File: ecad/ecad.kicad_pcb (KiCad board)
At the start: 4 copper layers, 130.5 x 110.5 mm, 122 parts, among them J1 JTAG, J2 USB_C, J3 Display, Q2 SS8050, SW1 Kailh choc v2, SW10 RotaryEncoder_Switch, SW11 RotaryEncoder_Switch, SW12 Kailh choc v2, SW13 Kailh choc v2, SW14 Kailh choc v2, SW15 RESET, SW16 Kailh choc v2, SW17 Kailh choc v2, SW18 Kailh choc v2, SW19 Kailh choc v2, SW2 Kailh choc v2, SW20 Kailh choc v2, SW21 Kailh choc v2, SW22 Kailh choc v2, SW23 Kailh choc v2, SW24 Kailh choc v2, SW25 Kailh choc v2, SW3 Kailh choc v2, SW4 Kailh choc v2, SW5 Kailh choc v2, SW6 Kailh choc v2, SW7 Kailh choc v2, SW8 Kailh choc v2, SW9 Kailh choc v2, U1 AP2112K-3.3, U2 RP2040, U4 SN74LV1T34DBV, U5 W25Q128JVP, Y1 12MHz

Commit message: fix(ecad): change screw placement and rounded corners
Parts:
- moved D29 104.7 mm to (190.7, 75.4)
- moved H1 70.0 mm to (125.7, 96.4)
- moved H3 68.5 mm to (125.7, 153.4)
- moved D46 34.0 mm to (205.8, 75.2), turned to 90 degrees
- moved H2 33.7 mm to (87.7, 96.4)
- moved H4 30.4 mm to (87.7, 153.4)
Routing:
- net GND: track 64.2 -> 64.9 mm, vias 43 -> 44
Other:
- outline, holes or cut-outs redrawn

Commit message: feat(ecad): ws2812b placement and routing
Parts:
- removed D15, D16, D20, D24, D28, D44: WS2812B-2020, LED_SMD:LED_WS2812B-2020_PLCC4_2.0x2.0mm
- added H10: MountingHole, MountingHole:MountingHole_2.2mm_M2_DIN965, F.Cu at (148.9, 169.8)
- added H11: MountingHole, MountingHole:MountingHole_2.2mm_M2_DIN965, F.Cu at (71.3, 73.4)
- added H12: MountingHole, MountingHole:MountingHole_2.2mm_M2_DIN965, F.Cu at (148.9, 73.4)
- added H9: MountingHole, MountingHole:MountingHole_2.2mm_M2_DIN965, F.Cu at (186.6, 100.2)
- moved D27 313.1 mm to (66.2, 78.8)
- moved D19 312.2 mm to (66.2, 121.6)
- moved D23 310.1 mm to (66.2, 99.8)
- moved D31 301.8 mm to (76.7, 174.9), turned to 0 degrees
- moved D30 274.3 mm to (97.7, 174.9), turned to 0 degrees
- moved D26 236.3 mm to (118.7, 174.9), turned to 0 degrees
- moved D22 199.9 mm to (138.2, 174.9), turned to 0 degrees
- moved D18 162.2 mm to (159.2, 174.9), turned to 0 degrees
- moved D47 154.4 mm to (66.2, 164.4), turned to -90 degrees
- moved D43 152.2 mm to (66.2, 143.4), turned to -90 degrees
- moved D42 146.0 mm to (76.7, 68.2)
- moved D14 124.9 mm to (180.2, 174.9), turned to 0 degrees
- moved D48 123.4 mm to (97.7, 68.2)
- moved D13 107.8 mm to (190.7, 164.4)
- moved D41 106.7 mm to (117.2, 68.2)
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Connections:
- D17 pad 1: Net-(D17-DOUT) -> Net-(D13-DIN)
- D23 pad 1: Net-(D19-DIN) -> Net-(D23-DOUT)
- D23 pad 3: Net-(D23-DIN) -> Net-(D19-DOUT)
- D27 pad 1: Net-(D23-DIN) -> Net-(D27-DOUT)
- D27 pad 3: Net-(D27-DIN) -> Net-(D23-DOUT)
- D31 pad 1: Net-(D27-DIN) -> Net-(D31-DOUT)
- D41 pad 3: Net-(D17-DOUT) -> Net-(D41-DIN)
- D42 pad 1: Net-(D13-DIN) -> Net-(D42-DOUT)
- D42 pad 2: unconnected-(D42-VSS-Pad2) -> GND
- D42 pad 3: Net-(D42-DIN) -> Net-(D27-DOUT)
- D43 pad 1: Net-(D43-DOUT) -> Net-(D19-DIN)
- D43 pad 3: Net-(D19-DOUT) -> Net-(D43-DIN)
- D46 pad 1: Net-(D42-DIN) -> unconnected-(D46-DOUT-Pad1)
- D46 pad 2: unconnected-(D46-VSS-Pad2) -> GND
- D47 pad 1: Net-(D47-DOUT) -> Net-(D43-DIN)
- D47 pad 3: Net-(D43-DOUT) -> Net-(D31-DOUT)
- D48 pad 1: Net-(D44-DIN) -> Net-(D41-DIN)
- D48 pad 3: Net-(D47-DOUT) -> Net-(D42-DOUT)
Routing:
- net +5V: track 8.41 -> 479.1 mm
- net Net-(D17-DIN): track 0.00 -> 20.5 mm
- net Net-(D19-DIN): track 0.00 -> 20.5 mm
- net Net-(D21-DIN): track 0.00 -> 20.5 mm
- net Net-(D19-DOUT): track 0.00 -> 20.5 mm
- net Net-(D43-DIN): track 0.00 -> 19.6 mm
- net Net-(D13-DIN): track 0.00 -> 19.6 mm
- net Net-(D42-DOUT): track 0.00 -> 19.6 mm
- net Net-(D41-DOUT): track 0.00 -> 19.6 mm
- net Net-(D30-DOUT): track 0.00 -> 19.6 mm
- net Net-(D26-DOUT): track 0.00 -> 19.6 mm
- net Net-(D45-DOUT): track 0.00 -> 19.6 mm
- net Net-(D25-DIN): track 0.00 -> 19.6 mm
- net Net-(D23-DOUT): track 0.00 -> 19.6 mm
- net Net-(D18-DOUT): track 0.00 -> 19.6 mm
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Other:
- board size 130.5 x 110.5 mm -> 130.5 x 112.7 mm

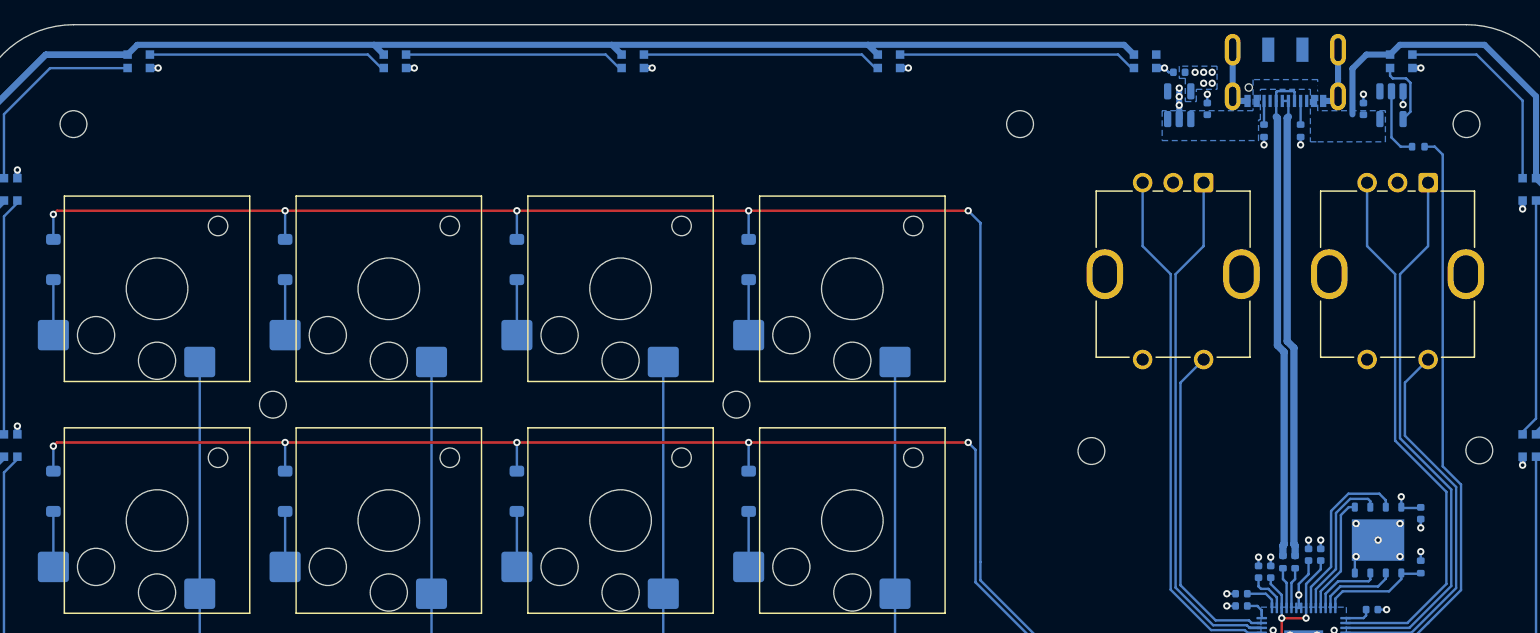
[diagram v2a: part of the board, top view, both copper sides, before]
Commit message: fix(ecad): change usb connector
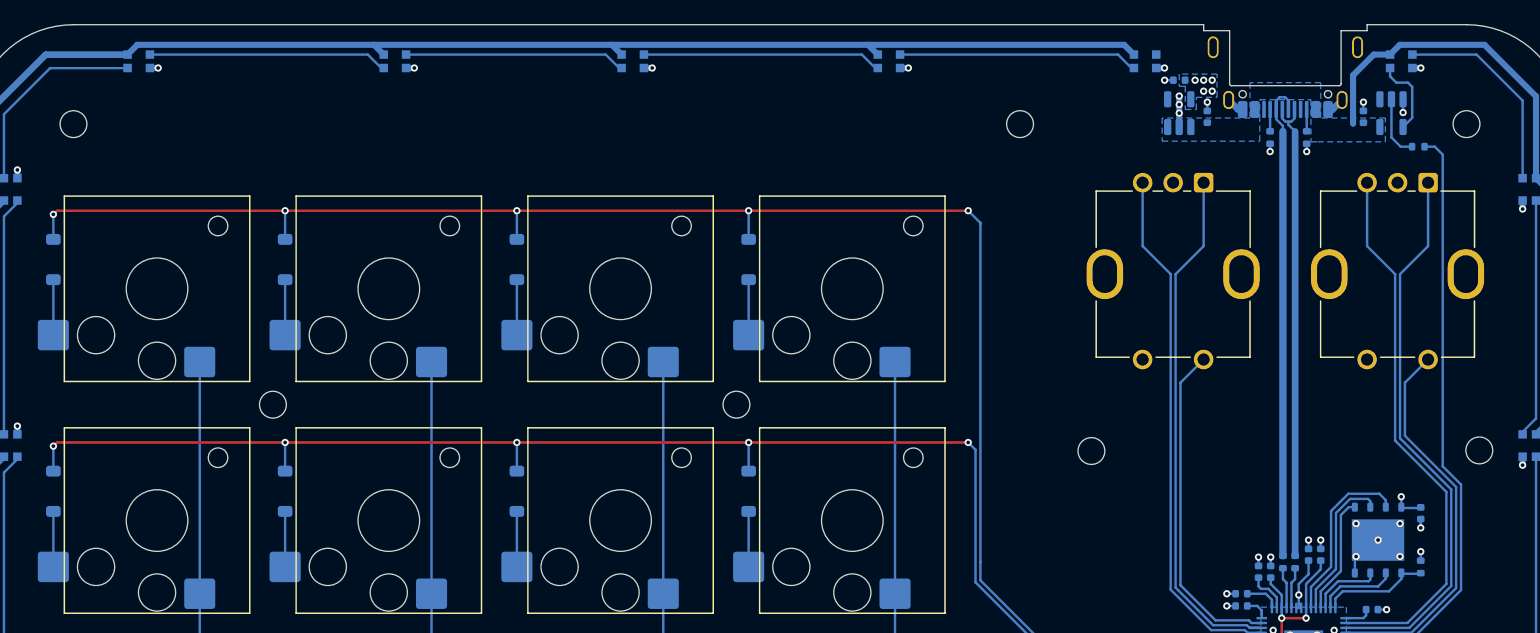
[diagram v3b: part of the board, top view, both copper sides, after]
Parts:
- J2: footprint Connector_USB:USB_C_Receptacle_JAE_DX07S016JA1R1500 -> Connector_USB:USB_C_Receptacle_Amphenol_12401948E412A
- moved J2 1.35 mm to (170.7, 67.1)
- moved R5 0.74 mm to (169.4, 74.5)
- moved R6 0.74 mm to (172.4, 74.5)
- moved U1 0.65 mm to (162.0, 72.5)
- moved U4 0.65 mm to (179.4, 72.5)
- moved C1 0.65 mm to (164.3, 72.8)
- moved C18 0.65 mm to (177.1, 72.8)
- moved C2 0.65 mm to (162.0, 69.8)
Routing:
- net GND: track 79.4 -> 71.8 mm, vias 64 -> 65
- net Net-(J2-D--PadA7): track 40.6 -> 39.5 mm
- net Net-(D32-DIN): track 5.77 -> 6.46 mm
- net Net-(U4-A): track 5.80 -> 5.15 mm
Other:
- outline, holes or cut-outs redrawn

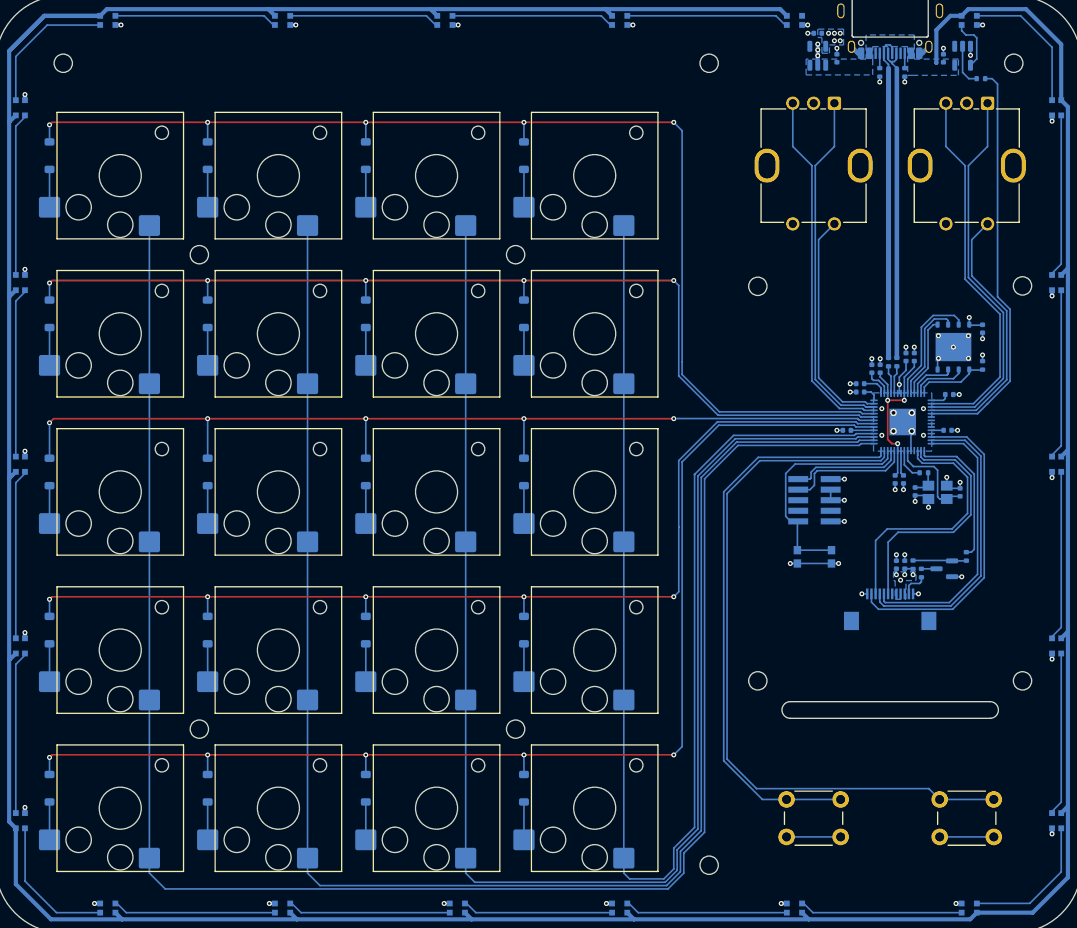
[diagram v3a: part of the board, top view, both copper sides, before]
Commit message: fix(ecad): change screw holes size
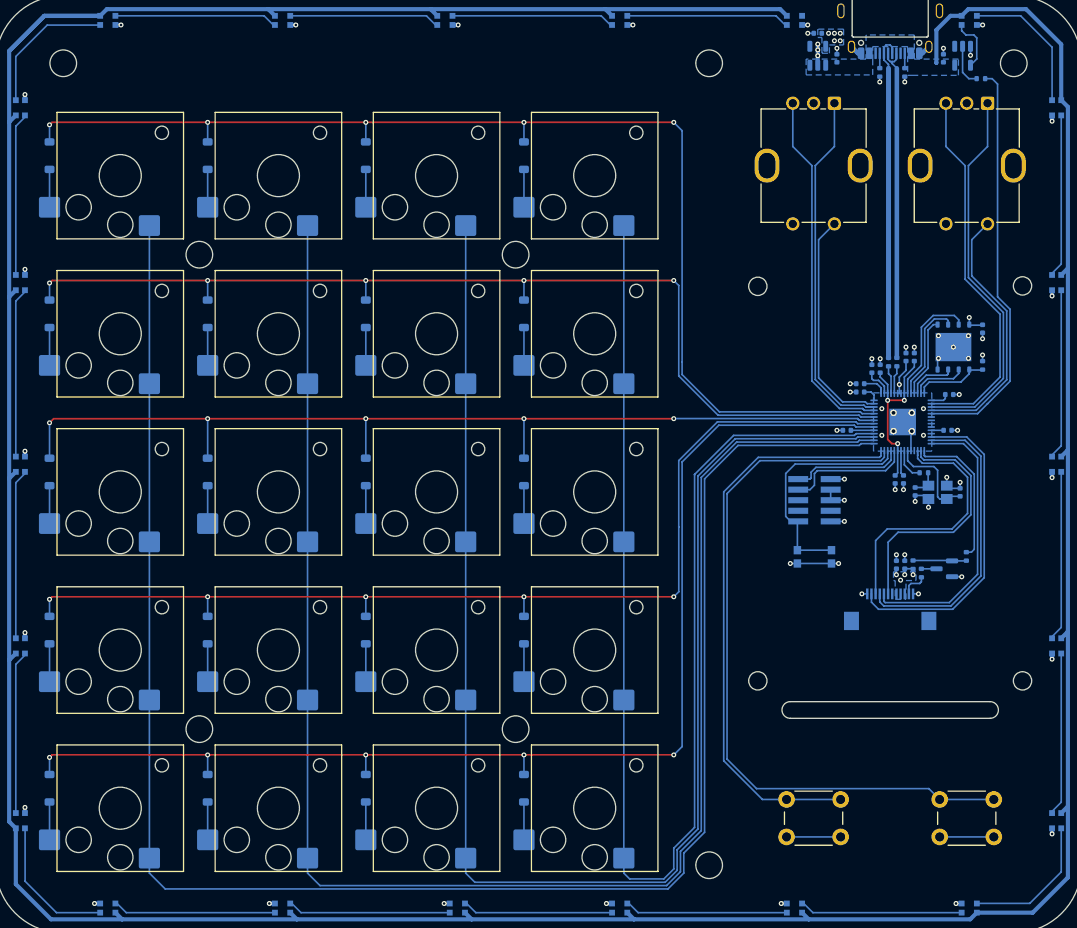
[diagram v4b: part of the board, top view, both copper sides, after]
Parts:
- H1, H10, H11, H12, H2, H3, H4, H5: footprint MountingHole:MountingHole_2.2mm_M2_DIN965 -> MountingHole:MountingHole_3.2mm_M3_DIN965
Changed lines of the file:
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@@
 	(net 104 "Net-(D43-DIN)")
 	(net 105 "Net-(D45-DOUT)")
-	(footprint "MountingHole:MountingHole_2.2mm_M2_DIN965"
+	(footprint "MountingHole:MountingHole_3.2mm_M3_DIN965"
 		(locked yes)
 		(layer "F.Cu")
 		(at 185.55 73.4)
-		(descr "Mounting Hole 2.2mm, M2, no annular, generated by kicad-footprint-generator mountinghole.py")
-		(tags "mountinghole M2 DIN965")
+		(descr "Mounting Hole 3.2mm, M3, no annular, generated by kicad-footprint-generator mountinghole.py")
+		(tags "mountinghole M3 DIN965")
 		(property "Reference" "H5"
-			(at 0 -2.85 0)
+			(at 0 -3.75 0)
 			(layer "F.SilkS")
 			(hide yes)
@@
 		)
 		(property "Value" "MountingHole"
-			(at 0 2.85 0)
+			(at 0 3.75 0)
 			(layer "F.Fab")
 			(effects
@@
 		(fp_circle
 			(center 0 0)
-			(end 1.9 0)
+			(end 2.8 0)
 			(stroke
 				(width 0.15)
@@
 		(fp_circle
 			(center 0 0)
-			(end 2.15 0)
+			(end 3.05 0)
 			(stroke
 				(width 0.05)
@@
 			(effects
 				(font
-					(size 0.95 0.95)
-					(thickness 0.14)
+					(size 1 1)
+					(thickness 0.15)
 				)
 			)
@@
 		(pad "" np_thru_hole circle
 			(at 0 0)
-			(size 2.2 2.2)
-			(drill 2.2)
+			(size 3.2 3.2)
+			(drill 3.2)
 			(layers "*.Cu" "*.Mask")
 		)
@@
 		)
 	)
-	(footprint "MountingHole:MountingHole_2.2mm_M2_DIN965"
+	(footprint "MountingHole:MountingHole_3.2mm_M3_DIN965"
 		(locked yes)
 		(layer "F.Cu")
 		(at 148.95 169.75)
-		(descr "Mounting Hole 2.2mm, M2, no annular, generated by kicad-footprint-generator mountinghole.py")
-		(tags "mountinghole M2 DIN965")
+		(descr "Mounting Hole 3.2mm, M3, no annular, generated by kicad-footprint-generator mountinghole.py")
+		(tags "mountinghole M3 DIN965")
 		(property "Reference" "H10"
-			(at 0 -2.85 0)
+			(at 0 -3.75 0)
 			(layer "F.SilkS")
 			(hide yes)
@@
 		)
 		(property "Value" "MountingHole"
-			(at 0 2.85 0)
+			(at 0 3.75 0)
 			(layer "F.Fab")
 			(effects
@@
 		(fp_circle
 			(center 0 0)
-			(end 1.9 0)
+			(end 2.8 0)
 			(stroke
 				(width 0.15)
@@
 		(fp_circle
 			(center 0 0)
-			(end 2.15 0)
+			(end 3.05 0)
 			(stroke
 				(width 0.05)
@@
 			(layer "F.CrtYd")
 		)
+		(fp_text user "${REFERENCE}"
+			(at 0 0 0)
+			(layer "F.Fab")
+			(effects
+				(font
+					(size 1 1)
+					(thickness 0.15)
+				)
+			)
+		)
 		(pad "" np_thru_hole circle
 			(at 0 0)
-			(size 2.2 2.2)
-			(drill 2.2)
+			(size 3.2 3.2)
+			(drill 3.2)
 			(layers "*.Cu" "*.Mask")
 		)
@@
 		)
 	)
-	(footprint "MountingHole:MountingHole_2.2mm_M2_DIN965"
+	(footprint "MountingHole:MountingHole_3.2mm_M3_DIN965"
 		(locked yes)
 		(layer "F.Cu")
 		(at 71.35 73.4)
-		(descr "Mounting Hole 2.2mm, M2, no annular, generated by kicad-footprint-generator mountinghole.py")
-		(tags "mountinghole M2 DIN965")
+		(descr "Mounting Hole 3.2mm, M3, no annular, generated by kicad-footprint-generator mountinghole.py")
+		(tags "mountinghole M3 DIN965")
 		(property "Reference" "H11"
-			(at 0 -2.85 0)
+			(at 0 -3.75 0)
 			(layer "F.SilkS")
 			(hide yes)
@@
 		)
 		(property "Value" "MountingHole"
-			(at 0 2.85 0)
+			(at 0 3.75 0)
 			(layer "F.Fab")
 			(effects
@@
 		(fp_circle
 			(center 0 0)
-			(end 1.9 0)
+			(end 2.8 0)
 			(stroke
 				(width 0.15)
@@
 		(fp_circle
 			(center 0 0)
-			(end 2.15 0)
+			(end 3.05 0)
 			(stroke
 				(width 0.05)
@@
 			(layer "F.CrtYd")
 		)
+		(fp_text user "${REFERENCE}"
+			(at 0 0 0)
+			(layer "F.Fab")
+			(effects
+				(font
+					(size 1 1)
+					(thickness 0.15)
+				)
+			)
+		)
 		(pad "" np_thru_hole circle
 			(at 0 0)
-			(size 2.2 2.2)
-			(drill 2.2)
+			(size 3.2 3.2)
+			(drill 3.2)
 			(layers "*.Cu" "*.Mask")
 		)
 		(embedded_fonts no)
 	)
-	(footprint "MountingHole:MountingHole_2.2mm_M2_DIN965"
+	(footprint "MountingHole:MountingHole_3.2mm_M3_DIN965"
 		(locked yes)
 		(layer "F.Cu")
 		(at 148.95 73.4)
-		(descr "Mounting Hole 2.2mm, M2, no annular, generated by kicad-footprint-generator mountinghole.py")
-		(tags "mountinghole M2 DIN965")
+		(descr "Mounting Hole 3.2mm, M3, no annular, generated by kicad-footprint-generator mountinghole.py")
+		(tags "mountinghole M3 DIN965")
 		(property "Reference" "H12"
-			(at 0 -2.85 0)
+			(at 0 -3.75 0)
 			(layer "F.SilkS")
 			(hide yes)
@@
 		)
 		(property "Value" "MountingHole"
-			(at 0 2.85 0)
+			(at 0 3.75 0)
 			(layer "F.Fab")
 			(effects
@@
 		(fp_circle
 			(center 0 0)
-			(end 1.9 0)
+			(end 2.8 0)
 			(stroke
 				(width 0.15)
@@
 		(fp_circle
 			(center 0 0)
-			(end 2.15 0)
+			(end 3.05 0)
 			(stroke
 				(width 0.05)
@@
 			(layer "F.CrtYd")
 		)
+		(fp_text user "${REFERENCE}"
+			(at 0 0 0)
+			(layer "F.Fab")
+			(effects
+				(font
+					(size 1 1)
+					(thickness 0.15)
+				)
+			)
+		)
 		(pad "" np_thru_hole circle
 			(at 0 0)
-			(size 2.2 2.2)
-			(drill 2.2)
+			(size 3.2 3.2)
+			(drill 3.2)
 			(layers "*.Cu" "*.Mask")
 		)
@@
 		)
 	)
-	(footprint "MountingHole:MountingHole_2.2mm_M2_DIN965"
+	(footprint "MountingHole:MountingHole_3.2mm_M3_DIN965"
 		(locked yes)
 		(layer "B.Cu")
 		(at 87.7 96.4 180)
-		(descr "Mounting Hole 2.2mm, M2, no annular, generated by kicad-footprint-generator mountinghole.py")
-		(tags "mountinghole M2 DIN965")
+		(descr "Mounting Hole 3.2mm, M3, no annular, generated by kicad-footprint-generator mountinghole.py")
+		(tags "mountinghole M3 DIN965")
 		(property "Reference" "H2"
-			(at 0 2.85 0)
+			(at 0 3.75 0)
 			(layer "B.SilkS")
 			(hide yes)
@@
 		)
 		(property "Value" "MountingHole"
-			(at 0 -2.85 0)
+			(at 0 -3.75 0)
 			(layer "B.Fab")
 			(effects
@@
 		(fp_circle
 			(center 0 0)
-			(end 1.9 0)
+			(end 2.8 0)
 			(stroke
 				(width 0.15)
@@
 		(fp_circle
 			(center 0 0)
-			(end 2.15 0)
+			(end 3.05 0)
 			(stroke
 				(width 0.05)
@@
 			(effects
 				(font
-					(size 0.95 0.95)
-					(thickness 0.14)
+					(size 1 1)
+					(thickness 0.15)
 				)
 				(justify mirror)
@@
 		(pad "" np_thru_hole circle
 			(at 0 0 180)
-			(size 2.2 2.2)
-			(drill 2.2)
+			(size 3.2 3.2)
+			(drill 3.2)
 			(layers "*.Cu" "*.Mask")
 		)
@@
 			)
 		)
+		(model "${KIPRJMOD}/3d/amphenol-12401948e412a.STEP"
+			(offset
+				(xyz 0 0 0)
+			)
+			(scale
+				(xyz 1 1 1)
+			)
+			(rotate
+				(xyz -90 -0 -0)
+			)
+		)
 	)
 	(footprint "Capacitor_SMD:C_0402_1005Metric"
@@
 		)
 	)
-	(footprint "MountingHole:MountingHole_2.2mm_M2_DIN965"
+	(footprint "MountingHole:MountingHole_3.2mm_M3_DIN965"
 		(locked yes)
 		(layer "B.Cu")
 		(at 87.7 153.4 180)
-		(descr "Mounting Hole 2.2mm, M2, no annular, generated by kicad-footprint-generator mountinghole.py")
-		(tags "mountinghole M2 DIN965")
+		(descr "Mounting Hole 3.2mm, M3, no annular, generated by kicad-footprint-generator mountinghole.py")
+		(tags "mountinghole M3 DIN965")
 		(property "Reference" "H4"
-			(at 0 2.85 0)
+			(at 0 3.75 0)
 			(layer "B.SilkS")
 			(hide yes)
@@
 		)
 		(property "Value" "MountingHole"
-			(at 0 -2.85 0)
+			(at 0 -3.75 0)
 			(layer "B.Fab")
 			(effects
@@
 		(fp_circle
 			(center 0 0)
-			(end 1.9 0)
+			(end 2.8 0)
 			(stroke
 				(width 0.15)
@@
 		(fp_circle
 			(center 0 0)
-			(end 2.15 0)
+			(end 3.05 0)
 			(stroke
 				(width 0.05)
@@
 			(effects
 				(font
-					(size 0.95 0.95)
-					(thickness 0.14)
+					(size 1 1)
+					(thickness 0.15)
 				)
 				(justify mirror)
@@
 		(pad "" np_thru_hole circle
 			(at 0 0 180)
-			(size 2.2 2.2)
-			(drill 2.2)
+			(size 3.2 3.2)
+			(drill 3.2)
 			(layers "*.Cu" "*.Mask")
 		)
@@
 		)
 	)
-	(footprint "MountingHole:MountingHole_2.2mm_M2_DIN965"
+	(footprint "MountingHole:MountingHole_3.2mm_M3_DIN965"
 		(locked yes)
 		(layer "B.Cu")
 		(at 125.7 96.4 180)
-		(descr "Mounting Hole 2.2mm, M2, no annular, generated by kicad-footprint-generator mountinghole.py")
-		(tags "mountinghole M2 DIN965")
+		(descr "Mounting Hole 3.2mm, M3, no annular, generated by kicad-footprint-generator mountinghole.py")
+		(tags "mountinghole M3 DIN965")
 		(property "Reference" "H1"
-			(at 0 2.85 0)
+			(at 0 3.75 0)
 			(layer "B.SilkS")
 			(hide yes)
@@
 		)
 		(property "Value" "MountingHole"
-			(at 0 -2.85 0)
+			(at 0 -3.75 0)
 			(layer "B.Fab")
 			(effects
@@
 		(fp_circle
 			(center 0 0)
-			(end 1.9 0)
+			(end 2.8 0)
 			(stroke
 				(width 0.15)
@@
 		(fp_circle
 			(center 0 0)
-			(end 2.15 0)
+			(end 3.05 0)
 			(stroke
 				(width 0.05)
@@
 			(effects
 				(font
-					(size 0.95 0.95)
-					(thickness 0.14)
+					(size 1 1)
+					(thickness 0.15)
 				)
 				(justify mirror)
@@
 		(pad "" np_thru_hole circle
 			(at 0 0 180)
-			(size 2.2 2.2)
-			(drill 2.2)
+			(size 3.2 3.2)
+			(drill 3.2)
 			(layers "*.Cu" "*.Mask")
 		)
@@
 		)
 	)
-	(footprint "MountingHole:MountingHole_2.2mm_M2_DIN965"
+	(footprint "MountingHole:MountingHole_3.2mm_M3_DIN965"
 		(locked yes)
 		(layer "B.Cu")
 		(at 125.7 153.4 180)
-		(descr "Mounting Hole 2.2mm, M2, no annular, generated by kicad-footprint-generator mountinghole.py")
-		(tags "mountinghole M2 DIN965")
+		(descr "Mounting Hole 3.2mm, M3, no annular, generated by kicad-footprint-generator mountinghole.py")
+		(tags "mountinghole M3 DIN965")
 		(property "Reference" "H3"
-			(at 0 2.85 0)
+			(at 0 3.75 0)
 			(layer "B.SilkS")
 			(hide yes)
@@
 		)
 		(property "Value" "MountingHole"
-			(at 0 -2.85 0)
+			(at 0 -3.75 0)
 			(layer "B.Fab")
 			(effects
@@
 		(fp_circle
 			(center 0 0)
-			(end 1.9 0)
+			(end 2.8 0)
 			(stroke
 				(width 0.15)
@@
 		(fp_circle
 			(center 0 0)
-			(end 2.15 0)
+			(end 3.05 0)
 			(stroke
 				(width 0.05)
@@
 			(effects
 				(font
-					(size 0.95 0.95)
-					(thickness 0.14)
+					(size 1 1)
+					(thickness 0.15)
 				)
 				(justify mirror)
@@
 		(pad "" np_thru_hole circle
 			(at 0 0 180)
-			(size 2.2 2.2)
-			(drill 2.2)
+			(size 3.2 3.2)
+			(drill 3.2)
 			(layers "*.Cu" "*.Mask")
 		)
